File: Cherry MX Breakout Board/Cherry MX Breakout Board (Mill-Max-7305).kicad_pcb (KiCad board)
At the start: 2 copper layers, 18.3 x 25.9 mm, 3 parts, among them J1 Conn_01x06_Male, U1 Cherry_MX_RGB

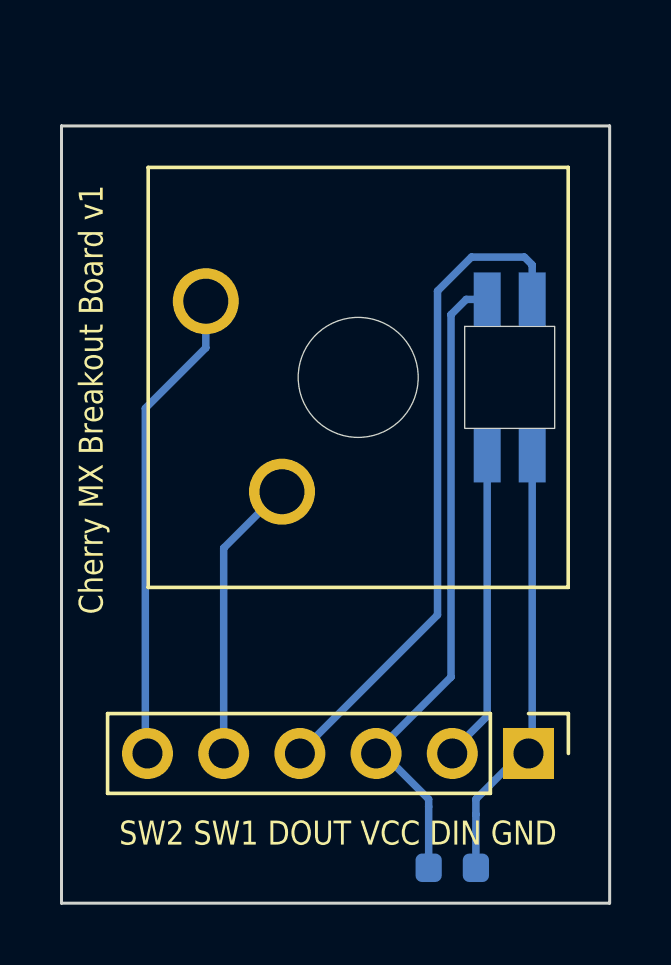
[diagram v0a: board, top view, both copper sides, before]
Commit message: Fix footprints and PCBs
- removed silkscreen of Cherry MX and Kailh Socket
- LTST-A683CEGBW pinout and model was rotated which caused invalid connections
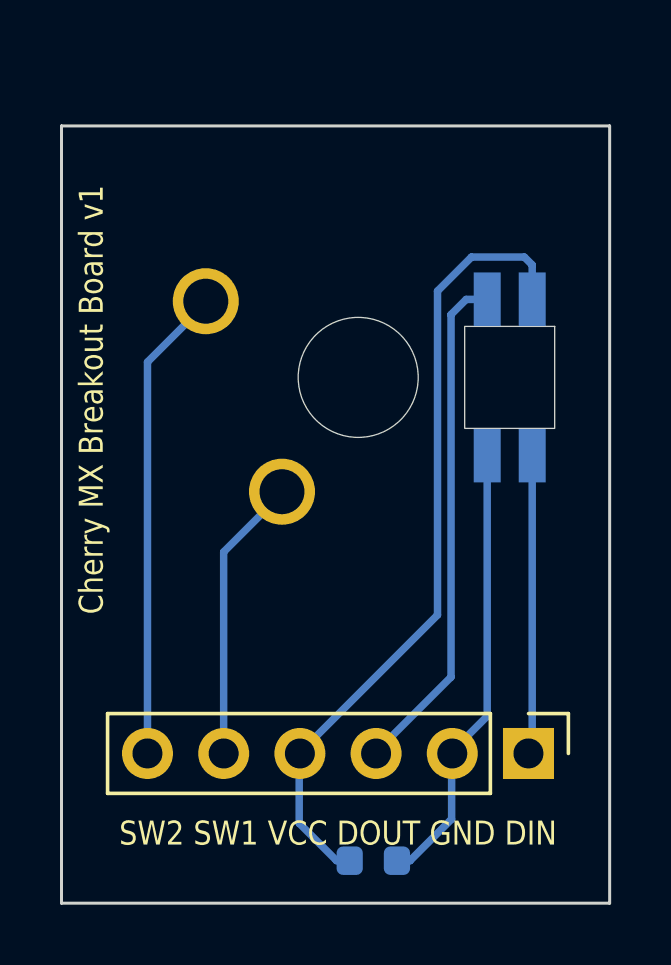
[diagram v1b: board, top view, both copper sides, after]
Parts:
- moved C1 2.64 mm to (153.9, 121.5)
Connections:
- J1 pad 1: GND -> DIN
- J1 pad 2: DIN -> GND
- J1 pad 3: VCC -> DOUT
- J1 pad 4: DOUT -> VCC
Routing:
- net DOUT: track 22.2 -> 17.0 mm
- net VCC: track 21.5 -> 26.7 mm
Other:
- board text added: "SW2 SW1 VCC DOUT GND DIN"
- board text removed: "SW2 SW1 DOUT VCC DIN GND"
